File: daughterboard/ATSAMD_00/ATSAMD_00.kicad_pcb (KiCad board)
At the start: 4 copper layers, 67 x 50 mm, 2 parts, among them J1 m2_keyA_67pin_daughterboard

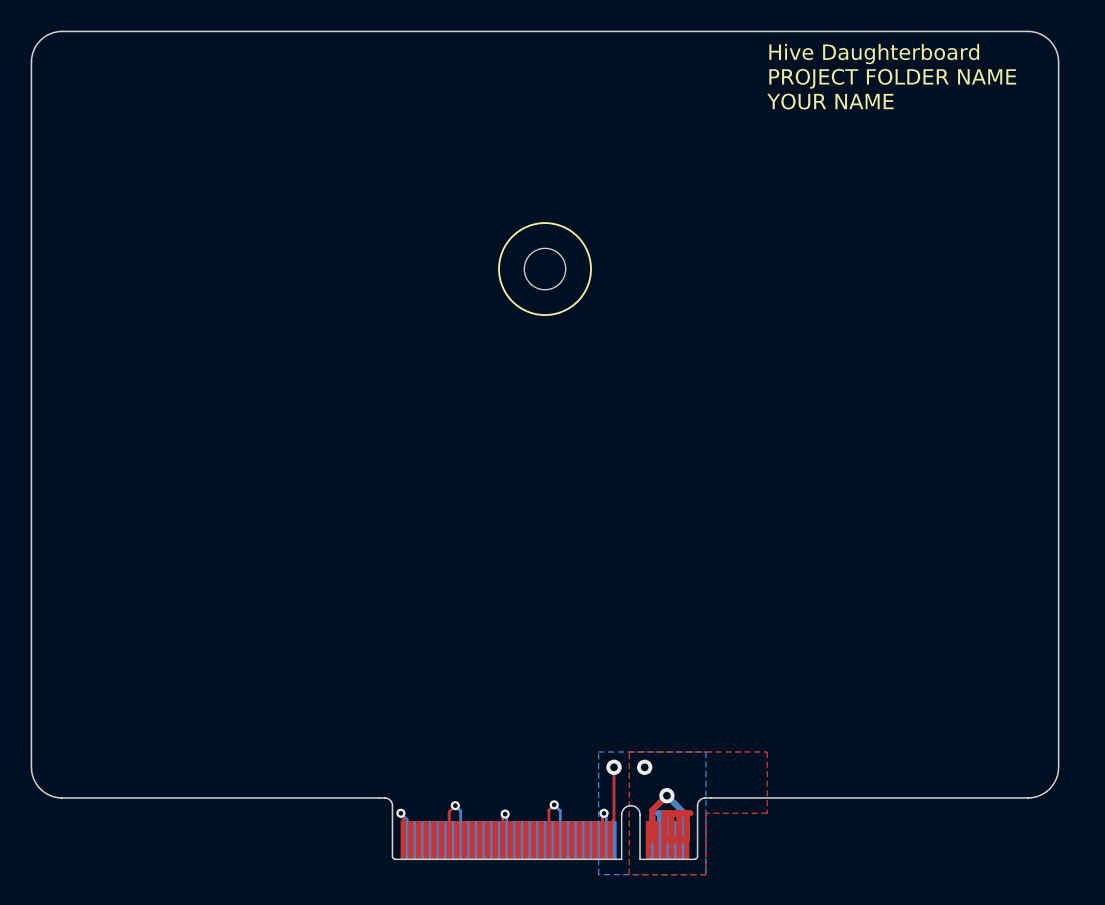
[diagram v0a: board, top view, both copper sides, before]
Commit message: finished ATSAMD daughterboard layout
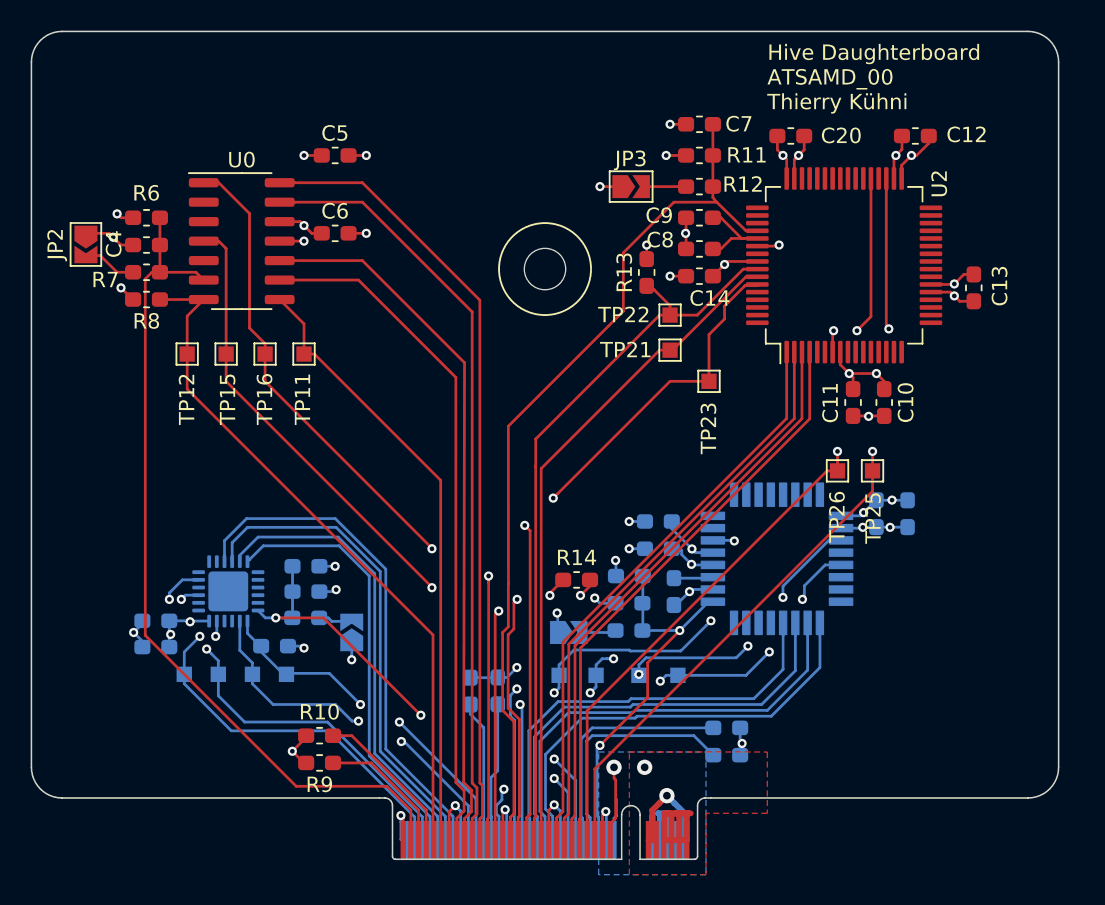
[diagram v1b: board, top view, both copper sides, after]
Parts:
- added C1: 100n, Capacitor_SMD:C_0603_1608Metric_Pad1.05x0.95mm_HandSolder, B.Cu at (132.9, 113.5)
- added C10: 10u, Capacitor_SMD:C_0603_1608Metric_Pad1.05x0.95mm_HandSolder, F.Cu at (170.6, 101.2)
- added C11: 1u, Capacitor_SMD:C_0603_1608Metric_Pad1.05x0.95mm_HandSolder, F.Cu at (168.6, 101.2)
- added C12: 100n, Capacitor_SMD:C_0603_1608Metric_Pad1.05x0.95mm_HandSolder, F.Cu at (172.7, 83.8)
- added C13: 100n, Capacitor_SMD:C_0603_1608Metric_Pad1.05x0.95mm_HandSolder, F.Cu at (176.5, 93.7)
- added C14: 100n, Capacitor_SMD:C_0603_1608Metric_Pad1.05x0.95mm_HandSolder, F.Cu at (158.6, 93.0)
- added C15: 100n, Capacitor_SMD:C_0603_1608Metric_Pad1.05x0.95mm_HandSolder, B.Cu at (154.0, 114.3)
- added C16: 1u, Capacitor_SMD:C_0603_1608Metric_Pad1.05x0.95mm_HandSolder, B.Cu at (156.9, 113.5)
- added C17: 10u, Capacitor_SMD:C_0603_1608Metric_Pad1.05x0.95mm_HandSolder, B.Cu at (172.2, 108.5)
- added C18: 100n, Capacitor_SMD:C_0603_1608Metric_Pad1.05x0.95mm_HandSolder, B.Cu at (155.9, 110.7)
- added C19: 100n, Capacitor_SMD:C_0603_1608Metric_Pad1.05x0.95mm_HandSolder, B.Cu at (170.1, 108.5)
- added C2: 4.7u, Capacitor_SMD:C_0603_1608Metric_Pad1.05x0.95mm_HandSolder, B.Cu at (123.1, 117.2)
- added C20: 100n, Capacitor_SMD:C_0603_1608Metric_Pad1.05x0.95mm_HandSolder, F.Cu at (164.5, 83.8)
- added C3: 100n, Capacitor_SMD:C_0603_1608Metric_Pad1.05x0.95mm_HandSolder, B.Cu at (123.1, 115.4)
- added C4: 100n, Capacitor_SMD:C_0603_1608Metric_Pad1.05x0.95mm_HandSolder, F.Cu at (122.5, 90.9)
- added C5: 4.7u, Capacitor_SMD:C_0603_1608Metric_Pad1.05x0.95mm_HandSolder, F.Cu at (134.8, 85.1)
- added C6: 100n, Capacitor_SMD:C_0603_1608Metric_Pad1.05x0.95mm_HandSolder, F.Cu at (134.8, 90.2)
- added C7: 100n, Capacitor_SMD:C_0603_1608Metric_Pad1.05x0.95mm_HandSolder, F.Cu at (158.6, 83.1)
- added C8: 100n, Capacitor_SMD:C_0603_1608Metric_Pad1.05x0.95mm_HandSolder, F.Cu at (158.6, 91.2)
- added C9: 4.7u, Capacitor_SMD:C_0603_1608Metric_Pad1.05x0.95mm_HandSolder, F.Cu at (158.6, 89.2)
- added JP1: NRST, Jumper:SolderJumper-2_P1.3mm_Open_TrianglePad1.0x1.5mm, B.Cu at (135.9, 116.2)
- added JP2: NRST, Jumper:SolderJumper-2_P1.3mm_Open_TrianglePad1.0x1.5mm, F.Cu at (118.6, 90.9)
- added JP3: NRST, Jumper:SolderJumper-2_P1.3mm_Open_TrianglePad1.0x1.5mm, F.Cu at (154.1, 87.1)
- added JP4: NRST, Jumper:SolderJumper-2_P1.3mm_Open_TrianglePad1.0x1.5mm, B.Cu at (150.1, 116.2)
- added R1: 10k, Resistor_SMD:R_0603_1608Metric_Pad1.05x0.95mm_HandSolder, B.Cu at (132.9, 111.9)
- added R10: 100k, Resistor_SMD:R_0603_1608Metric_Pad1.05x0.95mm_HandSolder, F.Cu at (133.8, 122.9)
- added R11: 10k, Resistor_SMD:R_0603_1608Metric_Pad1.05x0.95mm_HandSolder, F.Cu at (158.6, 85.1)
- added R12: 330, Resistor_SMD:R_0603_1608Metric_Pad1.05x0.95mm_HandSolder, F.Cu at (158.6, 87.1)
- added R13: 1k, Resistor_SMD:R_0603_1608Metric_Pad1.05x0.95mm_HandSolder, F.Cu at (155.1, 92.7)
- added R14: 100k, Resistor_SMD:R_0603_1608Metric_Pad1.05x0.95mm_HandSolder, F.Cu at (150.6, 112.8)
- added R15: 10k, Resistor_SMD:R_0603_1608Metric_Pad1.05x0.95mm_HandSolder, B.Cu at (154.0, 112.5)
- added R16: 330, Resistor_SMD:R_0603_1608Metric_Pad1.05x0.95mm_HandSolder, B.Cu at (154.0, 116.1)
- added R17: 1k, Resistor_SMD:R_0603_1608Metric_Pad1.05x0.95mm_HandSolder, B.Cu at (155.9, 109.0)
- added R18: 100k, Resistor_SMD:R_0603_1608Metric_Pad1.05x0.95mm_HandSolder, B.Cu at (160.4, 124.2)
- added R19: 100k, Resistor_SMD:R_0603_1608Metric_Pad1.05x0.95mm_HandSolder, B.Cu at (160.4, 122.4)
- added R2: 330, Resistor_SMD:R_0603_1608Metric_Pad1.05x0.95mm_HandSolder, B.Cu at (132.9, 115.3)
- added R3: 1k, Resistor_SMD:R_0603_1608Metric_Pad1.05x0.95mm_HandSolder, B.Cu at (130.9, 117.1)
- added R4: 100k, Resistor_SMD:R_0603_1608Metric_Pad1.05x0.95mm_HandSolder, B.Cu at (145.4, 120.0)
- added R5: 100k, Resistor_SMD:R_0603_1608Metric_Pad1.05x0.95mm_HandSolder, B.Cu at (143.6, 120.0)
- added R6: 10k, Resistor_SMD:R_0603_1608Metric_Pad1.05x0.95mm_HandSolder, F.Cu at (122.5, 89.2)
- added R7: 330, Resistor_SMD:R_0603_1608Metric_Pad1.05x0.95mm_HandSolder, F.Cu at (122.5, 92.7)
- added R8: 1k, Resistor_SMD:R_0603_1608Metric_Pad1.05x0.95mm_HandSolder, F.Cu at (122.5, 94.5)
- added R9: 100k, Resistor_SMD:R_0603_1608Metric_Pad1.05x0.95mm_HandSolder, F.Cu at (133.8, 124.7)
- added TP1: SWDIO, TestPoint:TestPoint_Pad_1.0x1.0mm, B.Cu at (129.4, 118.9)
- added TP11: SWDIO, TestPoint:TestPoint_Pad_1.0x1.0mm, F.Cu at (132.8, 98.0)
- added TP12: SWCLK, TestPoint:TestPoint_Pad_1.0x1.0mm, F.Cu at (125.2, 98.0)
- added TP15: USART_TX, TestPoint:TestPoint_Pad_1.0x1.0mm, F.Cu at (127.7, 98.0)
- added TP16: USART_RX, TestPoint:TestPoint_Pad_1.0x1.0mm, F.Cu at (130.2, 98.0)
- added TP2: SWCLK, TestPoint:TestPoint_Pad_1.0x1.0mm, B.Cu at (131.6, 118.9)
- added TP21: SWDIO, TestPoint:TestPoint_Pad_1.0x1.0mm, F.Cu at (156.7, 97.8)
- added TP22: SWCLK, TestPoint:TestPoint_Pad_1.0x1.0mm, F.Cu at (156.7, 95.5)
- added TP23: SWO, TestPoint:TestPoint_Pad_1.0x1.0mm, F.Cu at (159.2, 99.8)
- added TP25: USART_TX, TestPoint:TestPoint_Pad_1.0x1.0mm, F.Cu at (169.9, 105.7)
- added TP26: USART_RX, TestPoint:TestPoint_Pad_1.0x1.0mm, F.Cu at (167.6, 105.7)
- added TP31: SWDIO, TestPoint:TestPoint_Pad_1.0x1.0mm, B.Cu at (149.4, 119.0)
- added TP32: SWCLK, TestPoint:TestPoint_Pad_1.0x1.0mm, B.Cu at (151.8, 119.0)
- added TP35: USART_TX, TestPoint:TestPoint_Pad_1.0x1.0mm, B.Cu at (154.6, 119.0)
- added TP36: USART_RX, TestPoint:TestPoint_Pad_1.0x1.0mm, B.Cu at (157.2, 119.0)
- added TP5: USART_TX, TestPoint:TestPoint_Pad_1.0x1.0mm, B.Cu at (125.0, 118.9)
- added TP6: USART_RX, TestPoint:TestPoint_Pad_1.0x1.0mm, B.Cu at (127.2, 118.9)
- added U0: ATSAMD10C13A-SS, Package_SO:SOIC-14_3.9x8.7mm_P1.27mm, F.Cu at (128.7, 90.7)
- added U1: ATSAMD09D14A-M, Package_DFN_QFN:QFN-24-1EP_4x4mm_P0.5mm_EP2.6x2.6mm, B.Cu at (127.8, 113.5)
- added U2: ATSAMD51J18A-A, Package_QFP:TQFP-64_10x10mm_P0.5mm, F.Cu at (168.0, 92.3)
- added U3: ATSAMD21E16L-AFT, hive_daughterboard:ATSAMD21E16L-AFT, B.Cu at (163.6, 111.4)
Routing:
- net /Target 2/RST_2: track 0.00 -> 58.0 mm
- net /Target 0/RST_0: track 0.00 -> 55.0 mm
- net GND: track 28.1 -> 81.9 mm, vias 6 -> 34
- net /Target 0/UART_TxD0: track 0.00 -> 52.3 mm, vias 0 -> 2
- net /Target 0/GPIO0.3: track 0.00 -> 51.6 mm
- net /Target 2/UART_TxD2: track 0.00 -> 51.2 mm, vias 0 -> 2
- net /Target 2/UART_RxD2: track 0.00 -> 51.2 mm, vias 0 -> 2
- net /Target 0/GPIO0.2: track 0.00 -> 50.2 mm
- net /Target 0/UART_RxD0: track 0.00 -> 49.4 mm, vias 0 -> 2
- net /Target 2/TCK|SWDCLK_2: track 0.00 -> 47.8 mm
- net +3V3: track 11.6 -> 58.1 mm, vias 2 -> 23
- net /Target 0/GPIO0.1: track 0.00 -> 46.4 mm
- net /Target 0/TCK|SWDCLK_0: track 0.00 -> 45.2 mm
- net /Target 2/TDO|SWO_2: track 0.00 -> 44.8 mm, vias 0 -> 2
- net /Target 0/GPIO0.0: track 0.00 -> 44.7 mm
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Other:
- board text added: "Hive Daughterboard ATSAMD_00 Thierry Kühni"
- board text removed: "Hive Daughterboard PROJECT FOLDER NAME YOUR NAME"

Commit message: length matching daughterboards
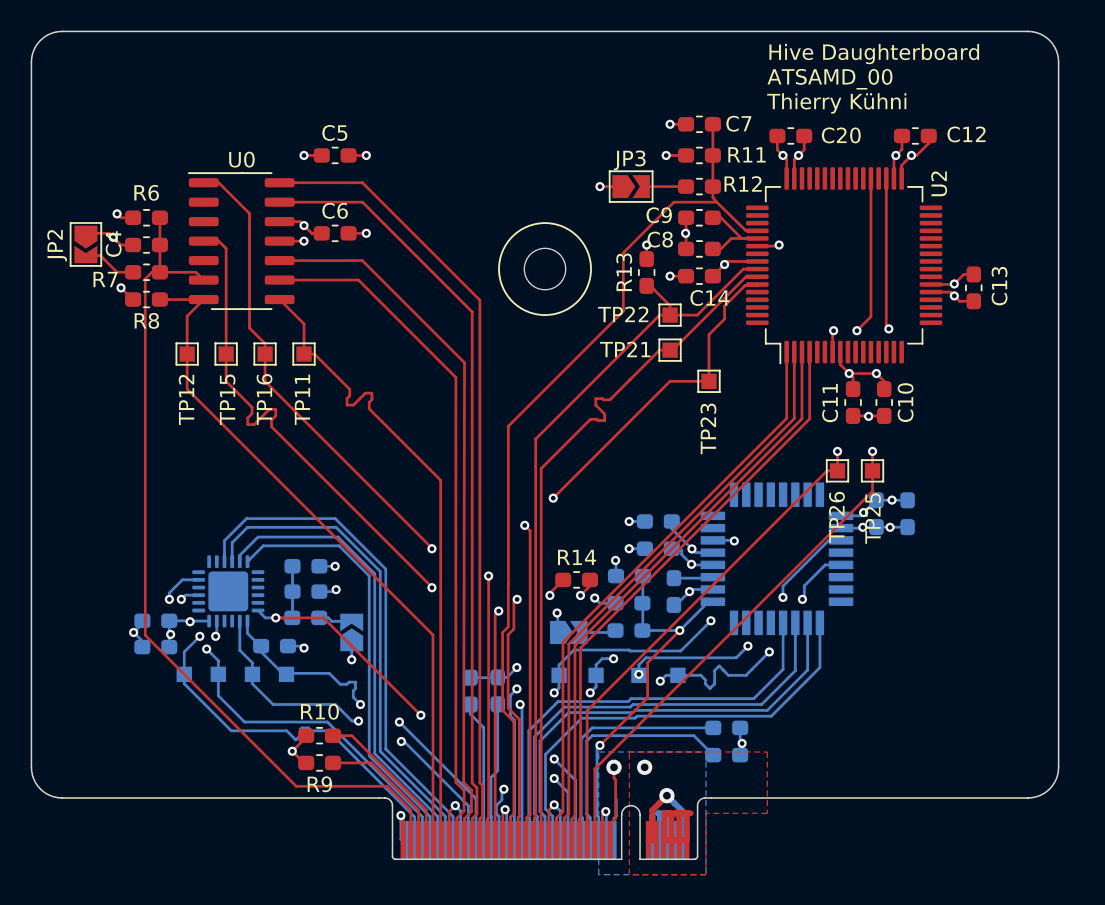
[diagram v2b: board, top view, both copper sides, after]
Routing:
- net /Target 3/TCK|SWDCLK_3: track 27.5 -> 34.6 mm
- net /Target 0/UART_RxD0: track 49.4 -> 52.3 mm
- net /Target 0/TMS|SWDIO_0: track 40.0 -> 42.4 mm
- net /Target 3/UART_TxD3: track 34.8 -> 36.7 mm
- net /Target 2/TMS|SWDIO_2: track 43.5 -> 45.3 mm
- net /Target 1/TCK|SWDCLK_1: track 23.2 -> 24.1 mm
- net /Target 1/UART_RxD1: track 27.8 -> 28.7 mm
